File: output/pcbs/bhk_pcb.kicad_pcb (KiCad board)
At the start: 2 copper layers, 164.2 x 123.2 mm, 116 parts

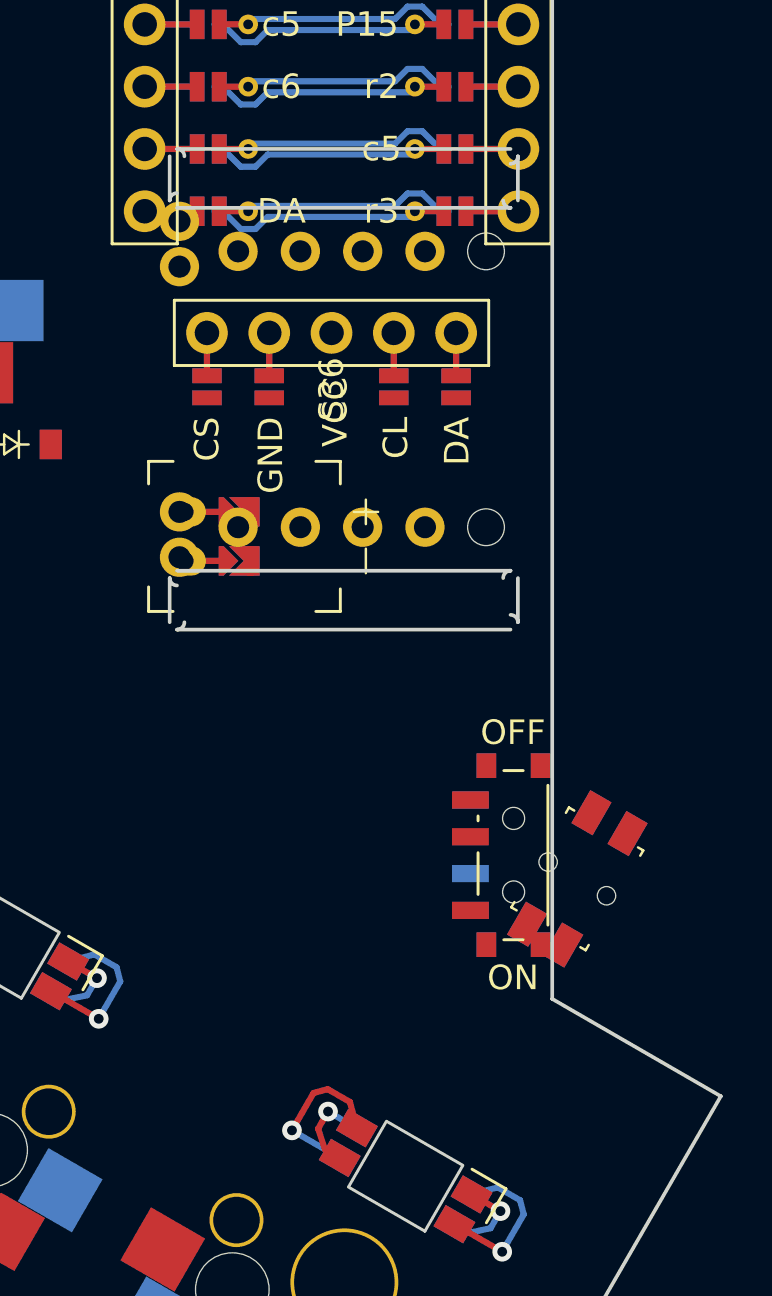
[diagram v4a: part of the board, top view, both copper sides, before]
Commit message: outline adjustment and pcn placement
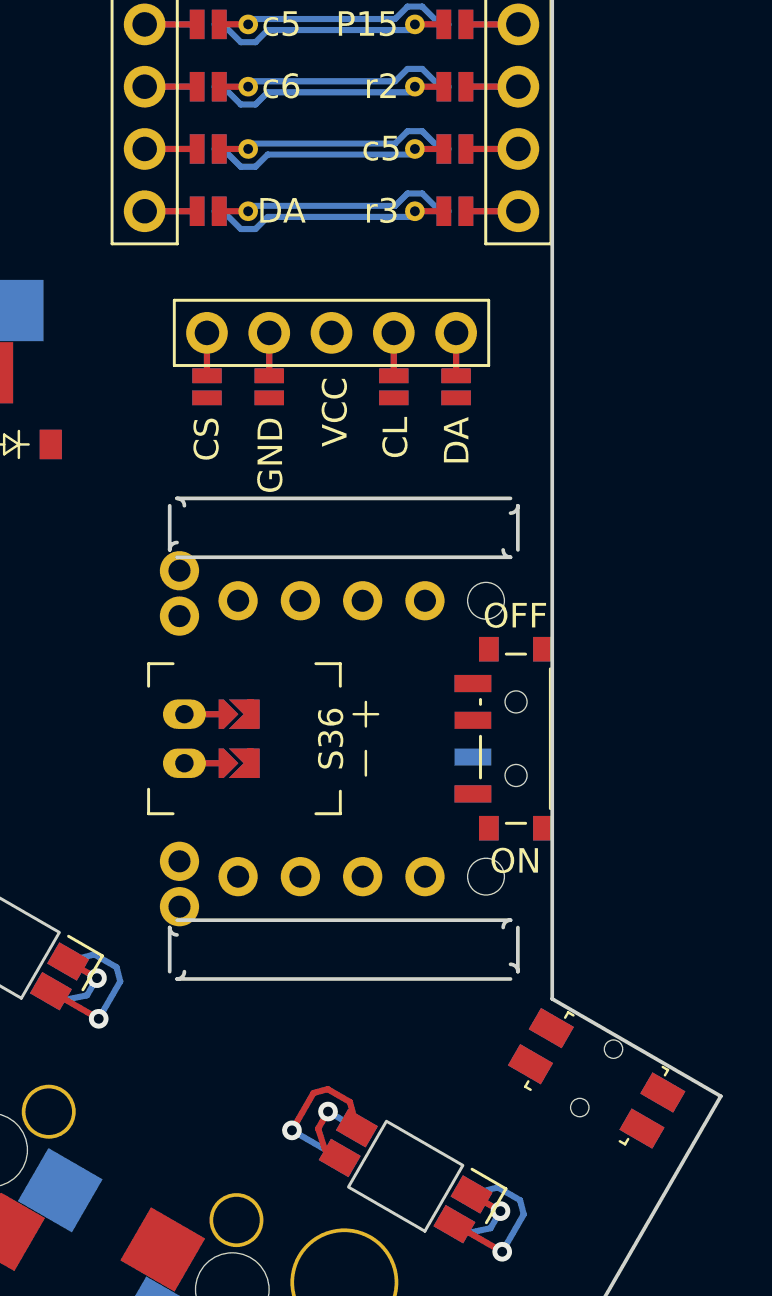
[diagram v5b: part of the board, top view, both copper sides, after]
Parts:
- moved S36 14.2 mm to (286.5, 124.9)
- moved JST1 8.25 mm to (280.5, 124.9)
- moved RST1 8.17 mm to (297.3, 138.7), turned to -30 degrees
- moved PWR1 4.75 mm to (294.0, 124.9)
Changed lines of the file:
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@@
   (segment (start 291.555 108.325) (end 291.555 110.075) (width 0.25) (layer "B.Cu") (net 82))
       (footprint "bhkfp:scrollwheel" (layer "F.Cu")
-      (at 286.475 110.625 90)
+      (at 286.475 124.875 90)
       (property "Reference" "S36" (at 0 0 90) (layer "F.SilkS")
         (effects (font (size 1 1) (thickness 0.15)))
@@
     (footprint "ceoloide:battery_connector_jst_ph_2"
         (layer "F.Cu")
-        (at 280.475 116.625 90)
+        (at 280.475 124.875 90)
         (property "Reference" "JST1"
             (at 0 4.8 90)
@@
         )
     )
-    (segment (start 282.27500000000003 117.625) (end 280.475 117.625) (width 0.25) (layer "F.Cu") (net 85))
-    (segment (start 282.27500000000003 117.625) (end 280.475 117.625) (width 0.25) (layer "B.Cu") (net 85))
-    (segment (start 282.27500000000003 115.625) (end 280.475 115.625) (width 0.25) (layer "F.Cu") (net 86))
-    (segment (start 282.27500000000003 115.625) (end 280.475 115.625) (width 0.25) (layer "B.Cu") (net 86))
+    (segment (start 282.27500000000003 125.875) (end 280.475 125.875) (width 0.25) (layer "F.Cu") (net 85))
+    (segment (start 282.27500000000003 125.875) (end 280.475 125.875) (width 0.25) (layer "B.Cu") (net 85))
+    (segment (start 282.27500000000003 123.875) (end 280.475 123.875) (width 0.25) (layer "F.Cu") (net 86))
+    (segment (start 282.27500000000003 123.875) (end 280.475 123.875) (width 0.25) (layer "B.Cu") (net 86))
   (footprint "ceoloide:power_switch_smd_side"
     (layer "F.Cu")
-    (at 293.875 129.625 0)
+    (at 293.975 124.875 0)
     (property "Reference" "PWR1"
       (at -3.6 0 -90)
@@
   (footprint "ceoloide:reset_switch_smd_side"
     (layer "F.Cu")
-    (at 296.49820109999996 130.59163579999998 60)
+    (at 297.2868218 138.7257048 -30)
     (property "Reference" "RST1"
-      (at 0 0 60)
+      (at 0 0 -30)
       (layer "F.SilkS")
       hide
@@
     (fp_line (start 1.3 -2.75) (end 1.3 -1.75) (stroke (width 0.1) (type solid)) (layer "Dwgs.User"))
     (fp_line (start 2.35 -1.75) (end 2.35 1.75) (stroke (width 0.1) (type solid)) (layer "Dwgs.User"))
-    (pad "" np_thru_hole circle (at 0 -1.375 240) (size 0.75 0.75) (drill 0.75) (layers "*.Cu" "*.Mask"))
-    (pad "" np_thru_hole circle (at 0 1.375 240) (size 0.75 0.75) (drill 0.75) (layers "*.Cu" "*.Mask"))
-    (pad "1" smd rect (at 2.625 -0.85 240) (size 1.55 1) (layers "F.Cu" "F.Paste" "F.Mask") (net 3 "GND"))
-    (pad "2" smd rect (at 2.625 0.85 240) (size 1.55 1) (layers "F.Cu" "F.Paste" "F.Mask") (net 45 "RST"))
-    (pad "3" smd rect (at -2.625 -0.85 240) (size 1.55 1) (layers "F.Cu" "F.Paste" "F.Mask") (net 3 "GND"))
-    (pad "4" smd rect (at -2.625 0.85 240) (size 1.55 1) (layers "F.Cu" "F.Paste" "F.Mask") (net 45 "RST"))
+    (pad "" np_thru_hole circle (at 0 -1.375 150) (size 0.75 0.75) (drill 0.75) (layers "*.Cu" "*.Mask"))
+    (pad "" np_thru_hole circle (at 0 1.375 150) (size 0.75 0.75) (drill 0.75) (layers "*.Cu" "*.Mask"))
+    (pad "1" smd rect (at 2.625 -0.85 150) (size 1.55 1) (layers "F.Cu" "F.Paste" "F.Mask") (net 3 "GND"))
+    (pad "2" smd rect (at 2.625 0.85 150) (size 1.55 1) (layers "F.Cu" "F.Paste" "F.Mask") (net 45 "RST"))
+    (pad "3" smd rect (at -2.625 -0.85 150) (size 1.55 1) (layers "F.Cu" "F.Paste" "F.Mask") (net 3 "GND"))
+    (pad "4" smd rect (at -2.625 0.85 150) (size 1.55 1) (layers "F.Cu" "F.Paste" "F.Mask") (net 45 "RST"))
     (fp_line (start -2.35 -1.5) (end -2.35 -1.75) (stroke (width 0.1) (type solid)) (layer "F.SilkS"))
     (fp_line (start -2.35 1.5) (end -2.35 1.75) (stroke (width 0.1) (type solid)) (layer "F.SilkS"))
@@
     (fp_line (start 2.35 -1.5) (end 2.35 -1.75) (stroke (width 0.1) (type solid)) (layer "F.SilkS"))
     (fp_line (start 2.35 1.5) (end 2.35 1.75) (stroke (width 0.1) (type solid)) (layer "F.SilkS"))
-    (pad "1" smd rect (at -2.625 -0.85 240) (size 1.55 1) (layers "B.Cu" "B.Paste" "B.Mask") (net 3 "GND"))
-    (pad "2" smd rect (at -2.625 0.85 240) (size 1.55 1) (layers "B.Cu" "B.Paste" "B.Mask") (net 45 "RST"))
-    (pad "3" smd rect (at 2.625 -0.85 240) (size 1.55 1) (layers "B.Cu" "B.Paste" "B.Mask") (net 3 "GND"))
-    (pad "4" smd rect (at 2.625 0.85 240) (size 1.55 1) (layers "B.Cu" "B.Paste" "B.Mask") (net 45 "RST"))
+    (pad "1" smd rect (at -2.625 -0.85 150) (size 1.55 1) (layers "B.Cu" "B.Paste" "B.Mask") (net 3 "GND"))
+    (pad "2" smd rect (at -2.625 0.85 150) (size 1.55 1) (layers "B.Cu" "B.Paste" "B.Mask") (net 45 "RST"))
+    (pad "3" smd rect (at 2.625 -0.85 150) (size 1.55 1) (layers "B.Cu" "B.Paste" "B.Mask") (net 3 "GND"))
+    (pad "4" smd rect (at 2.625 0.85 150) (size 1.55 1) (layers "B.Cu" "B.Paste" "B.Mask") (net 45 "RST"))
     (fp_line (start -2.35 -1.5) (end -2.35 -1.75) (stroke (width 0.1) (type solid)) (layer "B.SilkS"))
     (fp_line (start -2.35 1.5) (end -2.35 1.75) (stroke (width 0.1) (type solid)) (layer "B.SilkS"))

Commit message: fix ed some routing
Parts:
- removed D34, D35: , ceoloide:diode_tht_sod123
- removed LED34, LED35: , ceoloide:led_SK6812mini-e (per-key, reversible)
- removed S34, S35: , ceoloide:switch_mx
- removed S36: RollerEncoder_Panasonic_EVQWGD001, bhkfp:scrollwheel
- added C1: Capacitor_0603, Capacitor_0603, F.Cu at (150.0, 123.6)
- added C10: Capacitor_0603, Capacitor_0603, F.Cu at (228.4, 80.9)
- added C11: Capacitor_0603, Capacitor_0603, F.Cu at (247.4, 123.6)
- added C12: Capacitor_0603, Capacitor_0603, F.Cu at (247.4, 85.6)
- added C13: Capacitor_0603, Capacitor_0603, F.Cu at (266.4, 99.9)
- added C14: Capacitor_0603, Capacitor_0603, F.Cu at (274.2, 133.5)
- added C15: Capacitor_0603, Capacitor_0603, F.Cu at (290.7, 143.0)
- added C16: Capacitor_0603, Capacitor_0603, F.Cu at (150.0, 104.6)
- added C17: Capacitor_0603, Capacitor_0603, F.Cu at (150.0, 66.6)
- added C18: Capacitor_0603, Capacitor_0603, F.Cu at (171.4, 104.6)
- added C19: Capacitor_0603, Capacitor_0603, F.Cu at (171.4, 66.6)
- added C2: Capacitor_0603, Capacitor_0603, F.Cu at (150.0, 85.6)
- added C20: Capacitor_0603, Capacitor_0603, F.Cu at (190.4, 137.9)
- added C21: Capacitor_0603, Capacitor_0603, F.Cu at (190.4, 99.9)
- added C22: Capacitor_0603, Capacitor_0603, F.Cu at (190.4, 61.9)
- added C23: Capacitor_0603, Capacitor_0603, F.Cu at (209.4, 135.5)
- added C24: Capacitor_0603, Capacitor_0603, F.Cu at (209.4, 97.5)
- added C25: Capacitor_0603, Capacitor_0603, F.Cu at (209.4, 59.5)
- added C26: Capacitor_0603, Capacitor_0603, F.Cu at (228.4, 99.9)
- added C27: Capacitor_0603, Capacitor_0603, F.Cu at (228.4, 61.9)
- added C28: Capacitor_0603, Capacitor_0603, F.Cu at (247.4, 104.6)
- added C29: Capacitor_0603, Capacitor_0603, F.Cu at (247.4, 66.6)
- added C3: Capacitor_0603, Capacitor_0603, F.Cu at (171.4, 123.6)
- added C30: Capacitor_0603, Capacitor_0603, F.Cu at (266.4, 76.1)
- added C31: Capacitor_0603, Capacitor_0603, F.Cu at (239.8, 142.9)
- added C32: Capacitor_0603, Capacitor_0603, F.Cu at (262.4, 154.1)
- added C33: Capacitor_0603, Capacitor_0603, F.Cu at (278.8, 163.6)
- added C4: Capacitor_0603, Capacitor_0603, F.Cu at (171.4, 85.6)
- added C5: Capacitor_0603, Capacitor_0603, F.Cu at (190.4, 118.9)
- added C6: Capacitor_0603, Capacitor_0603, F.Cu at (190.4, 80.9)
- added C7: Capacitor_0603, Capacitor_0603, F.Cu at (209.4, 116.5)
- added C8: Capacitor_0603, Capacitor_0603, F.Cu at (209.4, 78.5)
- added C9: Capacitor_0603, Capacitor_0603, F.Cu at (228.4, 118.9)
- added H6: , ceoloide:mounting_hole_plated, F.Cu at (224.2, 141.7)
- added MOD1: , THQWGD001C, F.Cu at (286.5, 117.8)
- JST1: moved to B.Cu
- moved LED16 139.5 mm to (150.0, 107.0), turned to 180 degrees
- moved LED32 90.6 mm to (261.2, 156.2), turned to 150 degrees
- moved LED33 90.2 mm to (277.6, 165.7), turned to 150 degrees
- moved RST1 82.1 mm to (258.8, 66.2), turned to 0 degrees
- moved D30 81.6 mm to (262.4, 169.9), turned to 60 degrees
- moved S30 79.7 mm to (258.7, 160.5), turned to 150 degrees
- moved LED17 76.0 mm to (150.0, 69.0)
- moved PWR1 63.2 mm to (271.1, 65.9), turned to 90 degrees
- moved S5 60.9 mm to (171.4, 131.0)
- moved D5 59.7 mm to (179.4, 137.3), turned to 90 degrees
- moved LED28 59.0 mm to (247.4, 107.0)
- moved S14 57.8 mm to (209.4, 142.9)
- moved S15 57.8 mm to (209.4, 123.9)
- moved D14 56.6 mm to (217.4, 149.2), turned to 90 degrees
- moved D15 56.6 mm to (217.4, 130.2), turned to 90 degrees
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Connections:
- D1 pad 1: r5 -> r4
- D1 pad 2: c1_r5 -> c1_r4
- D10 pad 1: r1 -> r4
- D10 pad 2: c2_r1 -> c3_r4
- D11 pad 1: r5 -> r3
- D11 pad 2: c3_r5 -> c3_r3
- D12 pad 1: r4 -> r2
- D12 pad 2: c3_r4 -> c3_r2
- D13 pad 1: r3 -> r1
- D13 pad 2: c3_r3 -> c3_r1
- D14 pad 1: r2 -> r5
- D14 pad 2: c3_r2 -> c4_r5
- D15 pad 1: r1 -> r4
- D15 pad 2: c3_r1 -> c4_r4
- D16 pad 1: r5 -> r3
- D16 pad 2: c4_r5 -> c4_r3
- D17 pad 1: r4 -> r2
- D17 pad 2: c4_r4 -> c4_r2
- D18 pad 1: r3 -> r1
- D18 pad 2: c4_r3 -> c4_r1
- D19 pad 1: r2 -> r4
- D19 pad 2: c4_r2 -> c5_r4
- D2 pad 1: r4 -> r3
- D2 pad 2: c1_r4 -> c1_r3
- D20 pad 1: r1 -> r3
- D20 pad 2: c4_r1 -> c5_r3
- D21 pad 1: r4 -> r2
- D21 pad 2: c5_r4 -> c5_r2
- D22 pad 1: r3 -> r1
- D22 pad 2: c5_r3 -> c5_r1
- D23 pad 1: r2 -> r4
- D23 pad 2: c5_r2 -> c6_r4
- D24 pad 1: r1 -> r3
- D24 pad 2: c5_r1 -> c6_r3
- D25 pad 1: r4 -> r2
- D25 pad 2: c6_r4 -> c6_r2
- D26 pad 1: r3 -> r1
- D26 pad 2: c6_r3 -> c6_r1
- D27 pad 2: c6_r2 -> c7_r2
- D28 pad 2: c6_r1 -> c7_r1
- D29 pad 1: r2 -> r5
- D29 pad 2: c7_r2 -> c1_r2
- D3 pad 1: r3 -> r2
- D3 pad 2: c1_r3 -> c1_r2
- D30 pad 1: r1 -> r5
- D30 pad 2: c7_r1 -> c2_r2
- D31 pad 1: r5 -> r3
- D31 pad 2: c1_r2 -> c2_r1
- D32 pad 2: c2_r2 -> c3_r2
- D33 pad 1: r3 -> r4
- D33 pad 2: c2_r1 -> c3_r1
- D4 pad 1: r2 -> r1
- D4 pad 2: c1_r2 -> c1_r1
- D5 pad 1: r1 -> r4
- D5 pad 2: c1_r1 -> c2_r4
- D6 pad 1: r5 -> r3
- D6 pad 2: c2_r5 -> c2_r3
- D7 pad 1: r4 -> r2
- D7 pad 2: c2_r4 -> c2_r2
- D8 pad 1: r3 -> r1
- D8 pad 2: c2_r3 -> c2_r1
- D9 pad 1: r2 -> r5
- D9 pad 2: c2_r2 -> c3_r5
- LED14 pad 2: LED_31 -> LED_27
- LED14 pad 4: LED_30 -> LED_26
- LED15 pad 2: LED_32 -> LED_28
- LED15 pad 4: LED_31 -> LED_27
- LED16 pad 2: LED_34 -> LED_20
- LED16 pad 4: LED_33 -> LED_19
- LED17 pad 2: LED_27 -> LED_7
- LED17 pad 4: LED_26 -> LED_6
- LED18 pad 2: LED_15 -> LED_19
- LED18 pad 4: LED_14 -> LED_18
- LED19 pad 2: LED_7 -> LED_6
- LED19 pad 4: LED_6 -> LED_5
- LED20 pad 2: LED_28 -> LED_END
- LED20 pad 4: LED_27 -> LED_32
- LED21 pad 2: LED_16 -> LED_18
- LED21 pad 4: LED_15 -> LED_17
- LED22 pad 2: LED_6 -> LED_5
- LED22 pad 4: LED_5 -> LED_4
- LED23 pad 2: LED_29 -> LED_32
- LED23 pad 4: LED_28 -> LED_31
- LED25 pad 2: LED_5 -> LED_4
- LED25 pad 4: LED_4 -> LED_3
- LED26 pad 2: LED_30 -> LED_16
- LED26 pad 4: LED_29 -> LED_15
- LED27 pad 2: LED_18 -> LED_3
- LED27 pad 4: LED_17 -> LED_2
- LED28 pad 2: LED_4 -> LED_15
- LED28 pad 4: LED_3 -> LED_14
- LED29 pad 2: LED_19 -> LED_2
- LED29 pad 4: LED_18 -> LED_1
- LED30 pad 2: LED_3 -> LED_1
- LED30 pad 4: LED_2 -> DOUT
- LED31 pad 2: LED_20 -> LED_31
- LED31 pad 4: LED_19 -> LED_30
- LED32 pad 2: LED_2 -> LED_30
- LED32 pad 4: LED_1 -> LED_29
- LED33 pad 2: LED_1 -> LED_29
- LED33 pad 4: DOUT -> LED_28
- MCU1 pad 101: RAW -> DOUT
- MCU1 pad 102: GND -> c7
- MCU1 pad 103: RST -> GND
- MCU1 pad 104: VCC -> GND
- MCU1 pad 105: c6 -> r1
- MCU1 pad 106: (no net) -> c2
- MCU1 pad 107: r1 -> c3
- MCU1 pad 108: c6 -> c4
- MCU1 pad 109: P15 -> c5
- MCU1 pad 110: r2 -> c6
- MCU1 pad 111: c5 -> (no net)
- MCU1 pad 112: r3 -> DA
- MCU1 pad 113: DA -> r3
- MCU1 pad 114: (no net) -> c5
- MCU1 pad 115: c6 -> r2
- MCU1 pad 116: c5 -> P15
- MCU1 pad 117: c4 -> c6
- MCU1 pad 118: c3 -> r1
- MCU1 pad 119: c2 -> (no net)
- MCU1 pad 120: r1 -> c6
- MCU1 pad 121: GND -> VCC
- MCU1 pad 122: GND -> RST
- MCU1 pad 123: c7 -> GND
- MCU1 pad 124: DOUT -> RAW
- S1 pad : c1_r5 -> c1_r4
- S1 pad 1: c1_r5 -> c1_r4
- S10 pad : c2_r1 -> c3_r4
- S10 pad 1: c2_r1 -> c3_r4
- S10 pad 2: c2 -> c3
- S11 pad : c3_r5 -> c3_r3
- S11 pad 1: c3_r5 -> c3_r3
- S12 pad : c3_r4 -> c3_r2
- S12 pad 1: c3_r4 -> c3_r2
- S13 pad : c3_r3 -> c3_r1
- S13 pad 1: c3_r3 -> c3_r1
- S14 pad : c3_r2 -> c4_r5
- S14 pad 1: c3_r2 -> c4_r5
- S14 pad 2: c3 -> c4
- S15 pad : c3_r1 -> c4_r4
- S15 pad 1: c3_r1 -> c4_r4
- S15 pad 2: c3 -> c4
- S16 pad : c4_r5 -> c4_r3
- S16 pad 1: c4_r5 -> c4_r3
- S17 pad : c4_r4 -> c4_r2
- S17 pad 1: c4_r4 -> c4_r2
- S18 pad : c4_r3 -> c4_r1
- S18 pad 1: c4_r3 -> c4_r1
- S19 pad : c4_r2 -> c5_r4
- S19 pad 1: c4_r2 -> c5_r4
- S19 pad 2: c4 -> c5
- S2 pad : c1_r4 -> c1_r3
- S2 pad 1: c1_r4 -> c1_r3
- S20 pad : c4_r1 -> c5_r3
- S20 pad 1: c4_r1 -> c5_r3
- S20 pad 2: c4 -> c5
- S21 pad : c5_r4 -> c5_r2
- S21 pad 1: c5_r4 -> c5_r2
- S22 pad : c5_r3 -> c5_r1
- S22 pad 1: c5_r3 -> c5_r1
- S23 pad : c5_r2 -> c6_r4
- S23 pad 1: c5_r2 -> c6_r4
- S23 pad 2: c5 -> c6
- S24 pad : c5_r1 -> c6_r3
- S24 pad 1: c5_r1 -> c6_r3
- S24 pad 2: c5 -> c6
- S25 pad : c6_r4 -> c6_r2
- S25 pad 1: c6_r4 -> c6_r2
- S26 pad : c6_r3 -> c6_r1
- S26 pad 1: c6_r3 -> c6_r1
- S27 pad : c6_r2 -> c7_r2
- S27 pad 1: c6_r2 -> c7_r2
- S27 pad 2: c6 -> c7
- S28 pad : c6_r1 -> c7_r1
- S28 pad 1: c6_r1 -> c7_r1
- S28 pad 2: c6 -> c7
- S29 pad : c7_r2 -> c1_r2
- S29 pad 1: c7_r2 -> c1_r2
- S29 pad 2: c7 -> c5
- S3 pad : c1_r3 -> c1_r2
- S3 pad 1: c1_r3 -> c1_r2
- S30 pad : c7_r1 -> c2_r2
- S30 pad 1: c7_r1 -> c2_r2
- S30 pad 2: c7 -> c6
- S31 pad : c1_r2 -> c2_r1
- S31 pad 1: c1_r2 -> c2_r1
- S31 pad 2: c5 -> c7
- S32 pad : c2_r2 -> c3_r2
- S32 pad 1: c2_r2 -> c3_r2
- S32 pad 2: c6 -> c7
- S33 pad : c2_r1 -> c3_r1
- S33 pad 1: c2_r1 -> c3_r1
- S4 pad : c1_r2 -> c1_r1
- S4 pad 1: c1_r2 -> c1_r1
- S5 pad : c1_r1 -> c2_r4
- S5 pad 1: c1_r1 -> c2_r4
- S5 pad 2: c1 -> c2
- S6 pad : c2_r5 -> c2_r3
- S6 pad 1: c2_r5 -> c2_r3
- S7 pad : c2_r4 -> c2_r2
- S7 pad 1: c2_r4 -> c2_r2
- S8 pad : c2_r3 -> c2_r1
- S8 pad 1: c2_r3 -> c2_r1
- S9 pad : c2_r2 -> c3_r5
- S9 pad 1: c2_r2 -> c3_r5
- S9 pad 2: c2 -> c3
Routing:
- net (no net): track 333.1 -> 3412.2 mm, vias 0 -> 240
- net VCC: track 131.4 -> 0.00 mm, vias 35 -> 0
- net GND: track 131.4 -> 0.00 mm, vias 35 -> 0
- net LED_29: track 13.5 -> 0.00 mm, vias 2 -> 0
- net LED_28: track 13.5 -> 0.00 mm, vias 2 -> 0
- net LED_27: track 13.5 -> 0.00 mm, vias 2 -> 0
- net LED_26: track 13.5 -> 0.00 mm, vias 2 -> 0
- net LED_9: track 13.5 -> 0.00 mm, vias 2 -> 0
- net LED_8: track 13.5 -> 0.00 mm, vias 2 -> 0
- net LED_7: track 13.5 -> 0.00 mm, vias 2 -> 0
- net LED_6: track 13.5 -> 0.00 mm, vias 2 -> 0
- net LED_5: track 13.5 -> 0.00 mm, vias 2 -> 0
- net LED_4: track 13.5 -> 0.00 mm, vias 2 -> 0
- net LED_3: track 13.5 -> 0.00 mm, vias 2 -> 0
- net LED_25: track 13.5 -> 0.00 mm, vias 2 -> 0
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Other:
- board size 164.2 x 123.2 mm -> 164.2 x 125.6 mm

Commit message: update
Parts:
- added D34: , ceoloide:diode_tht_sod123, F.Cu at (294.5, 124.0)
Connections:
- net P8 renamed P20
- D29 pad 2: c1_r2 -> c5_r5
- D30 pad 1: r5 -> r4
- D30 pad 2: c2_r2 -> c7_r4
- D31 pad 1: r3 -> r5
- D31 pad 2: c2_r1 -> c6_r5
- D32 pad 1: r5 -> r4
- D32 pad 2: c3_r2 -> c8_r4
- D33 pad 1: r4 -> r5
- D33 pad 2: c3_r1 -> c8_r5
- MCU1 pad 111: (no net) -> c8
- S29 pad 1: c1_r2 -> c5_r5
- S30 pad 1: c2_r2 -> c7_r4
- S30 pad 2: c6 -> c7
- S31 pad 1: c2_r1 -> c6_r5
- S31 pad 2: c7 -> c6
- S32 pad 1: c3_r2 -> c8_r4
- S32 pad 2: c7 -> c8
- S33 pad 1: c3_r1 -> c8_r5
- S33 pad 2: c7 -> c8
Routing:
- added copper zone on F.Cu, net GND
